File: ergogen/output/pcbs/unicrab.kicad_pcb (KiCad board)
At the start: 2 copper layers, 230 x 104.3 mm, 72 parts

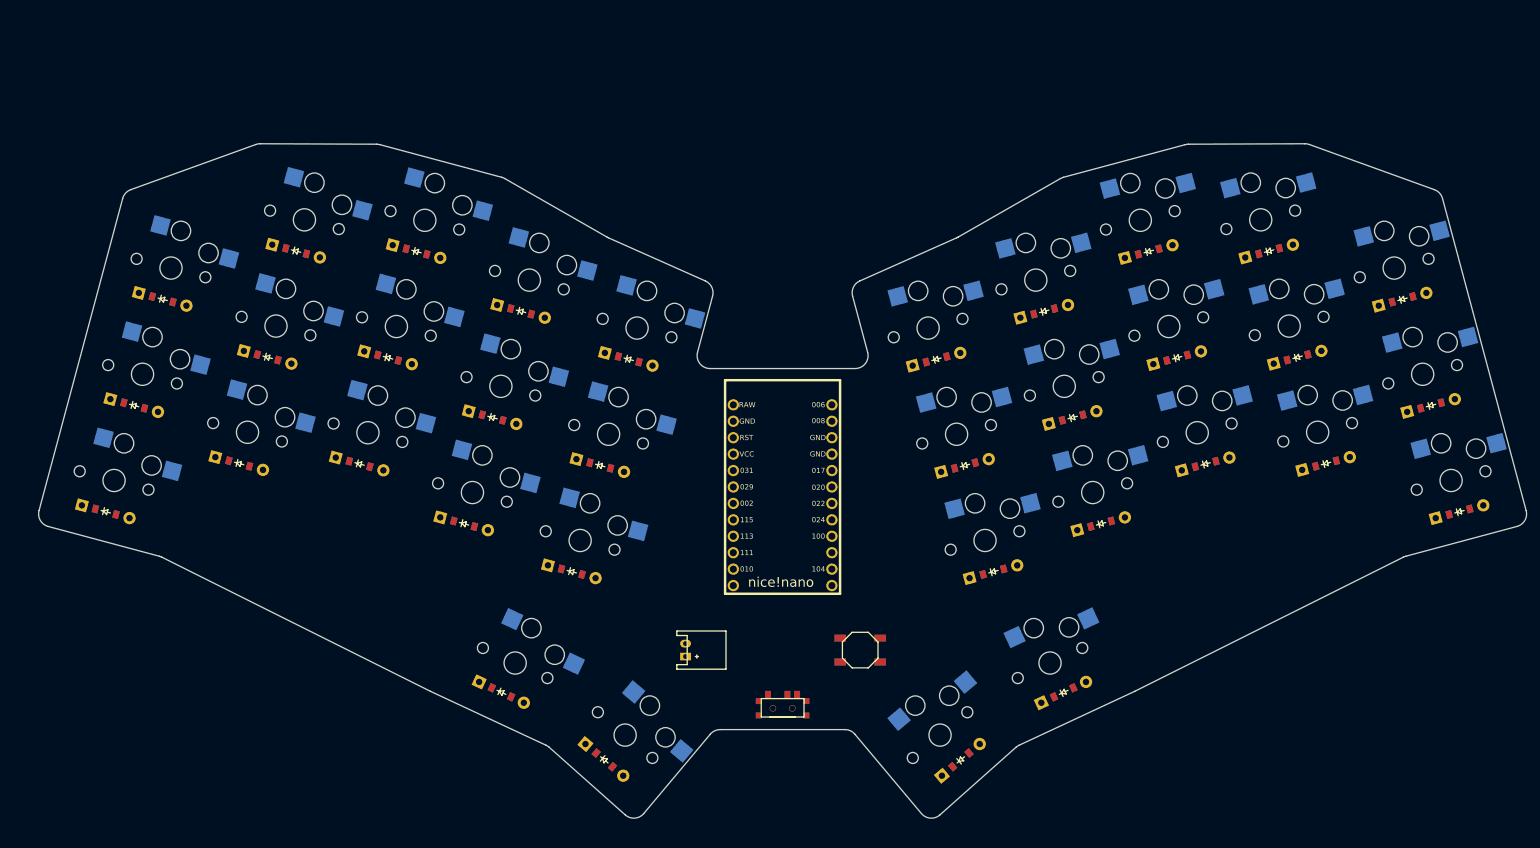
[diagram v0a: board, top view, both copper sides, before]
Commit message: wire the left side
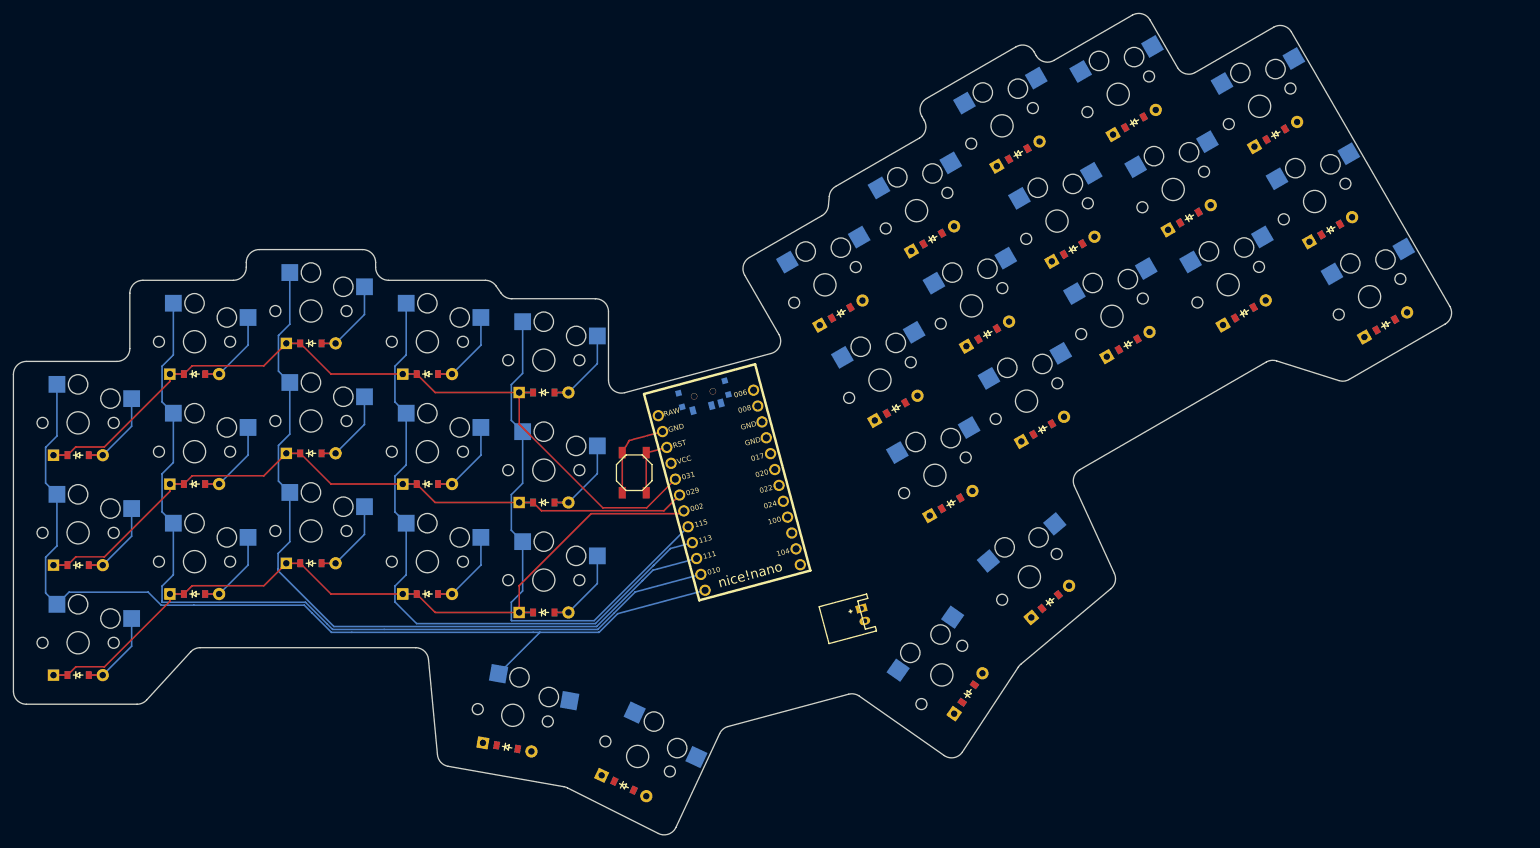
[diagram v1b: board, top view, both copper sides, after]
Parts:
- moved T1 50.1 mm to (161.8, 109.1), turned to 15 degrees
- moved B1 44.4 mm to (151.1, 121.3), turned to 90 degrees
- moved S20 32.5 mm to (247.8, 64.6), turned to 30 degrees
- moved D20 32.2 mm to (250.3, 69.0), turned to 30 degrees
- moved S19 31.5 mm to (256.3, 79.3), turned to 30 degrees
- moved D19 31.3 mm to (258.8, 83.7), turned to 30 degrees
- moved S18 31.1 mm to (264.8, 94.1), turned to 30 degrees
- moved D18 31.1 mm to (267.3, 98.4), turned to 30 degrees
- moved S23 29.4 mm to (226.0, 62.8), turned to 30 degrees
- moved D23 28.8 mm to (228.5, 67.1), turned to 30 degrees
- moved JST1 28.0 mm to (186.5, 143.2), turned to -75 degrees
- moved S3 27.9 mm to (65.1, 113.6), turned to 0 degrees
- moved S22 27.7 mm to (234.5, 77.5), turned to 30 degrees
- moved D3 27.4 mm to (65.1, 118.6), turned to 0 degrees
- moved D22 27.3 mm to (237.0, 81.8), turned to 30 degrees
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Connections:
- D1 pad 1: P029 -> P002
- D10 pad 1: P029 -> P002
- D11 pad 1: P031 -> P029
- D12 pad 1: P006 -> P031
- D13 pad 1: P029 -> P002
- D14 pad 1: P031 -> P029
- D15 pad 1: P006 -> P031
- D16 pad 1: P009 -> P104
- D17 pad 1: P009 -> P104
- D18 pad 1: P020 -> P022
- D19 pad 1: P017 -> P020
- D2 pad 1: P031 -> P029
- D20 pad 1: P008 -> P017
- D21 pad 1: P020 -> P022
- D22 pad 1: P017 -> P020
- D23 pad 1: P008 -> P017
- D24 pad 1: P020 -> P022
- D25 pad 1: P017 -> P020
- D26 pad 1: P008 -> P017
- D27 pad 1: P020 -> P022
- D28 pad 1: P017 -> P020
- D29 pad 1: P008 -> P017
- D3 pad 1: P006 -> P031
- D30 pad 1: P020 -> P022
- D31 pad 1: P017 -> P020
- D32 pad 1: P008 -> P017
- D4 pad 1: P029 -> P002
- D5 pad 1: P031 -> P029
- D6 pad 1: P006 -> P031
- D7 pad 1: P029 -> P002
- D8 pad 1: P031 -> P029
- D9 pad 1: P006 -> P031
- S1 pad 1: P010 -> P009
- S10 pad 1: P115 -> P113
- S11 pad 1: P115 -> P113
- S12 pad 1: P115 -> P113
- S13 pad 1: P002 -> P115
- S14 pad 1: P002 -> P115
- S15 pad 1: P002 -> P115
- S16 pad 1: P010 -> P009
- S17 pad 1: P111 -> P010
- S18 pad 1: P010 -> P009
- S19 pad 1: P010 -> P009
- S2 pad 1: P010 -> P009
- S20 pad 1: P010 -> P009
- S21 pad 1: P111 -> P010
- S22 pad 1: P111 -> P010
- S23 pad 1: P111 -> P010
- S24 pad 1: P113 -> P111
- S25 pad 1: P113 -> P111
- S26 pad 1: P113 -> P111
- S27 pad 1: P115 -> P113
- S28 pad 1: P115 -> P113
- S29 pad 1: P115 -> P113
- S3 pad 1: P010 -> P009
- S30 pad 1: P002 -> P115
- S31 pad 1: P002 -> P115
- S32 pad 1: P002 -> P115
- S33 pad 1: P010 -> P009
- S34 pad 1: P111 -> P010
- S4 pad 1: P111 -> P010
- S5 pad 1: P111 -> P010
- S6 pad 1: P111 -> P010
- S7 pad 1: P113 -> P111
- S8 pad 1: P113 -> P111
- S9 pad 1: P113 -> P111
- T1 pad 1: pos -> RAW
- T1 pad 2: RAW -> pos
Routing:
- net P009: track 0.00 -> 151.2 mm
- net P010: track 0.00 -> 137.6 mm
- net P031: track 0.00 -> 132.2 mm
- net P002: track 0.00 -> 130.3 mm
- net P111: track 0.00 -> 121.9 mm
- net P029: track 0.00 -> 120.1 mm
- net P113: track 0.00 -> 102.1 mm
- net P115: track 0.00 -> 83.2 mm
- net pinky_top: track 0.00 -> 14.9 mm
- net index_bottom: track 0.00 -> 14.9 mm
- net ring_top: track 0.00 -> 14.9 mm
- net index_top: track 0.00 -> 14.9 mm
- net inner_home: track 0.00 -> 14.9 mm
- net pinky_home: track 0.00 -> 14.9 mm
- net middle_bottom: track 0.00 -> 14.9 mm
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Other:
- board size 230 x 104.3 mm -> 222.3 x 127 mm
- net class Default removed

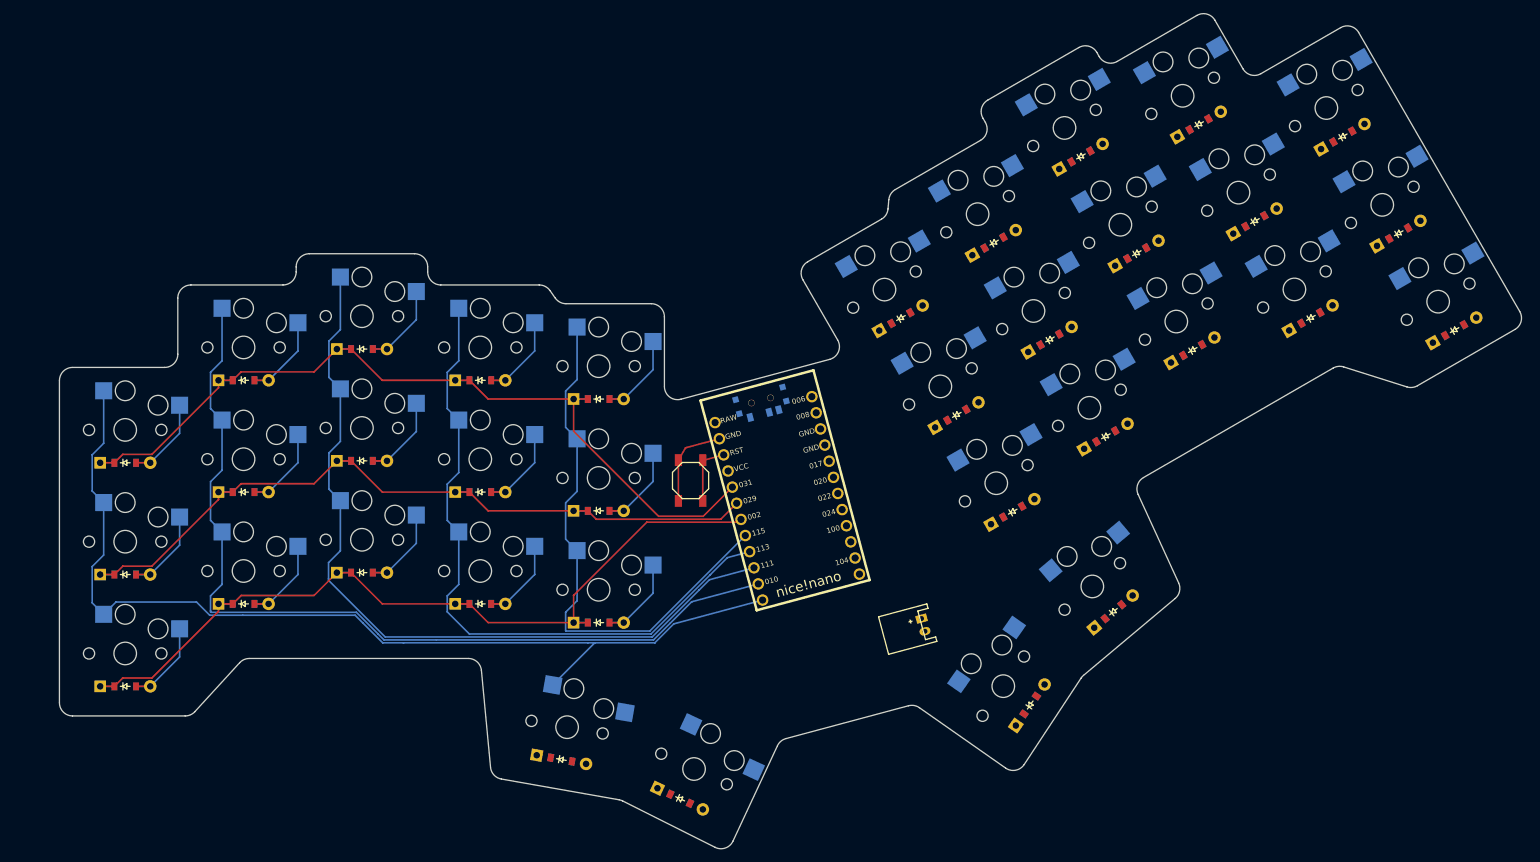
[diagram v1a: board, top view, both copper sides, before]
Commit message: wire middle components
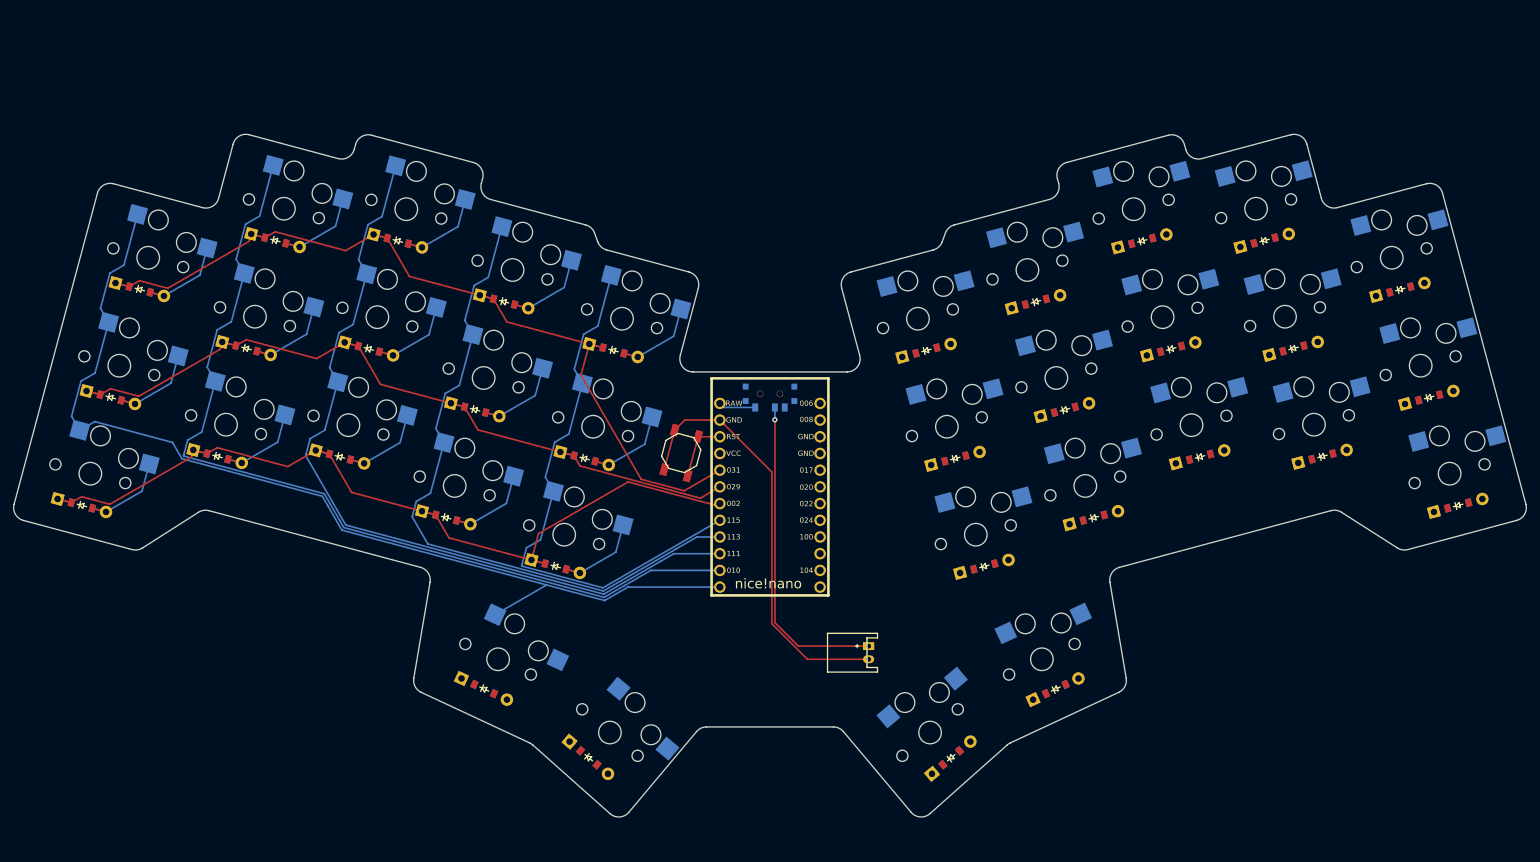
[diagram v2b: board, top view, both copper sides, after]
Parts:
- moved D1 28.3 mm to (58.6, 125.1), turned to -15 degrees
- moved S1 27.8 mm to (59.9, 120.2), turned to -15 degrees
- moved D2 27.0 mm to (63.0, 108.6), turned to -15 degrees
- moved S2 26.8 mm to (64.3, 103.8), turned to -15 degrees
- moved D18 26.7 mm to (267.9, 125.1), turned to 15 degrees
- moved D3 26.4 mm to (67.4, 92.2), turned to -15 degrees
- moved S3 26.4 mm to (68.7, 87.4), turned to -15 degrees
- moved S18 26.2 mm to (266.6, 120.2), turned to 15 degrees
- moved D19 25.4 mm to (263.5, 108.6), turned to 15 degrees
- moved S19 25.2 mm to (262.2, 103.8), turned to 15 degrees
- moved D20 24.9 mm to (259.1, 92.2), turned to 15 degrees
- moved S20 24.8 mm to (257.8, 87.4), turned to 15 degrees
- moved D4 22.8 mm to (79.2, 117.6), turned to -15 degrees
- moved S4 22.4 mm to (80.5, 112.8), turned to -15 degrees
- moved S6 22.0 mm to (89.3, 79.9), turned to -15 degrees
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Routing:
- net GND: track 13.7 -> 64.9 mm
- net pos: track 0.00 -> 48.5 mm, vias 0 -> 1
- net RAW: track 0.00 -> 5.63 mm
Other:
- board size 222.3 x 127 mm -> 230 x 103.8 mm

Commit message: wire the rest
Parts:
- moved D26 12.2 mm to (231.4, 80.9)
- moved S30 12.2 mm to (206.1, 125.6)
- moved S31 12.2 mm to (201.7, 109.2)
- moved S3 12.2 mm to (80.2, 83.5)
- moved D31 12.2 mm to (203.0, 114.0)
- moved D2 12.2 mm to (74.5, 104.7)
- moved D12 12.2 mm to (134.3, 90.2)
- moved B1 12.2 mm to (161.3, 113.2)
- moved S23 12.2 mm to (248.7, 76.0)
- moved D11 12.2 mm to (129.9, 106.6)
- moved D9 12.2 mm to (118.2, 80.9)
- moved S2 12.2 mm to (75.8, 99.9)
- moved S25 12.2 mm to (234.5, 92.5)
- moved S28 12.2 mm to (218.3, 101.8)
- moved D3 12.2 mm to (78.9, 88.3)
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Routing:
- net P010: track 137.6 -> 337.8 mm, vias 0 -> 1
- net P009: track 151.2 -> 312.8 mm
- net P022: track 0.00 -> 135.8 mm
- net P017: track 0.00 -> 134.9 mm
- net P111: track 121.9 -> 247.7 mm
- net P020: track 0.00 -> 112.9 mm
- net P113: track 102.1 -> 208.0 mm
- net P115: track 83.2 -> 171.4 mm
- net P104: track 0.00 -> 76.3 mm, vias 0 -> 1
- net P106: track 0.00 -> 66.4 mm
- net GND: track 64.9 -> 83.7 mm
- net reachy_cluster: track 0.00 -> 15.1 mm
- net tucky_cluster: track 0.00 -> 15.1 mm
- net mirror_tucky_cluster: track 0.00 -> 14.9 mm
- net mirror_reachy_cluster: track 0.00 -> 14.9 mm
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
